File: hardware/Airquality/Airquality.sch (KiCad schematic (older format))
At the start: 6 parts, among them J1 Conn_01x04_Female, J2 Conn_01x04_Female, U1 WeMos_D1_mini, U2 DS18B20, U3 PMS7003

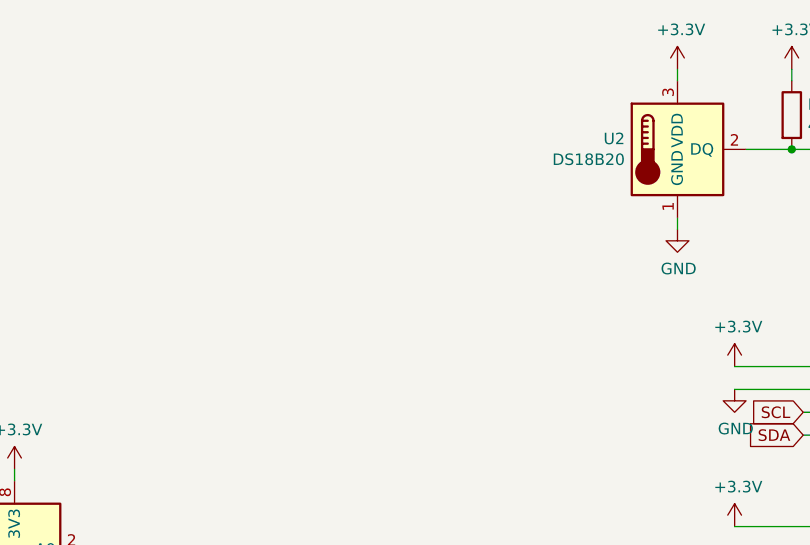
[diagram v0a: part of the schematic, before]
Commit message: added 4 pinheaders for aliexpress i2c sensor modules
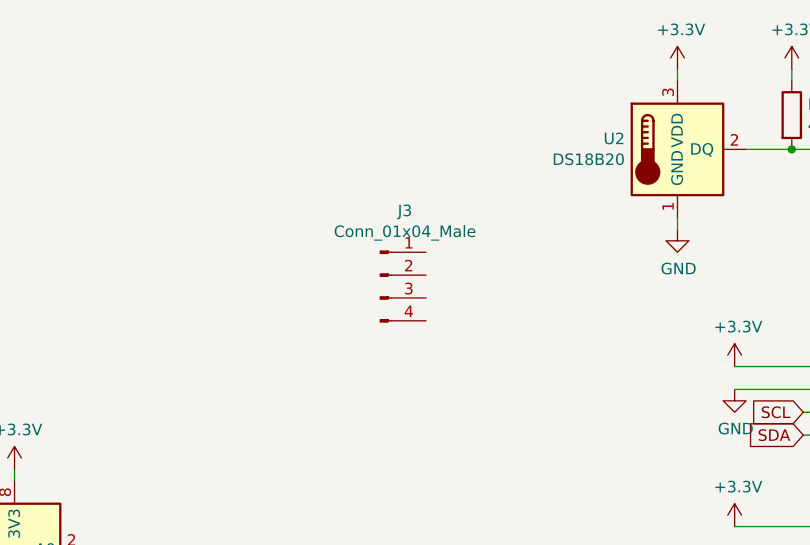
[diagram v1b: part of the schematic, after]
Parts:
- added J3: Conn_01x04_Male, Connector:NS-Tech_Grove_1x04_P2mm_Vertical, symbol Connector:Conn_01x04_Male
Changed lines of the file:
@@
 Wire Wire Line
 	8150 950  8150 1000
+$Comp
+L Connector:Conn_01x04_Male J3
+U 1 1 5ED64641
+P 6350 1850
+F 0 "J3" H 6458 2131 50  0000 C CNN
+F 1 "Conn_01x04_Male" H 6458 2040 50  0000 C CNN
+F 2 "Connector:NS-Tech_Grove_1x04_P2mm_Vertical" H 6350 1850 50  0001 C CNN
+F 3 "~" H 6350 1850 50  0001 C CNN
+	1    6350 1850
+	1    0    0    -1
+$EndComp
 $EndSCHEMATC
